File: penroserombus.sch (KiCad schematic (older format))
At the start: 11 parts, among them J1 Conn_01x03_Female, J2 Conn_01x03_Female, J3 Conn_01x03_Male, J4 Conn_01x03_Male, SW1 SW_DPDT_x2

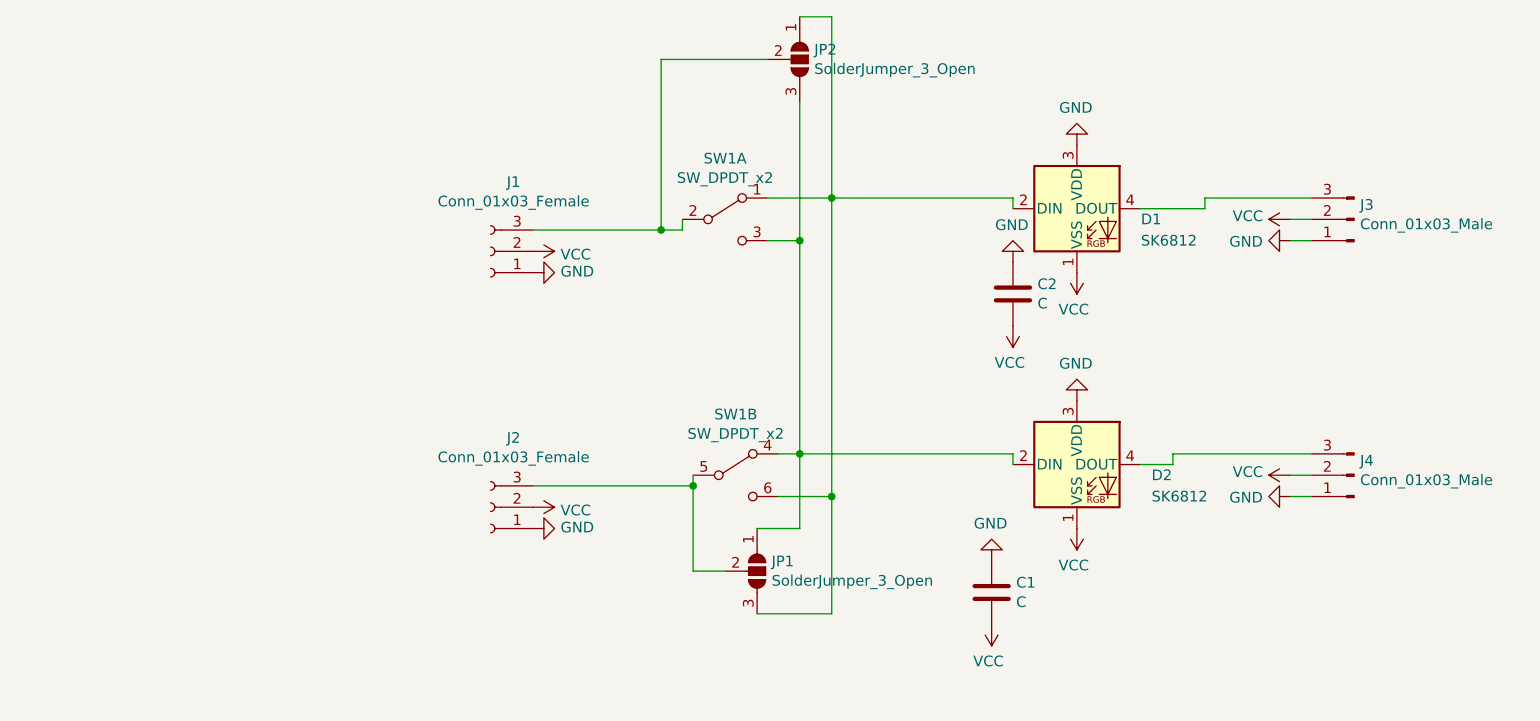
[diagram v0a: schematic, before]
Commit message: board has 4 leds instead of 2.
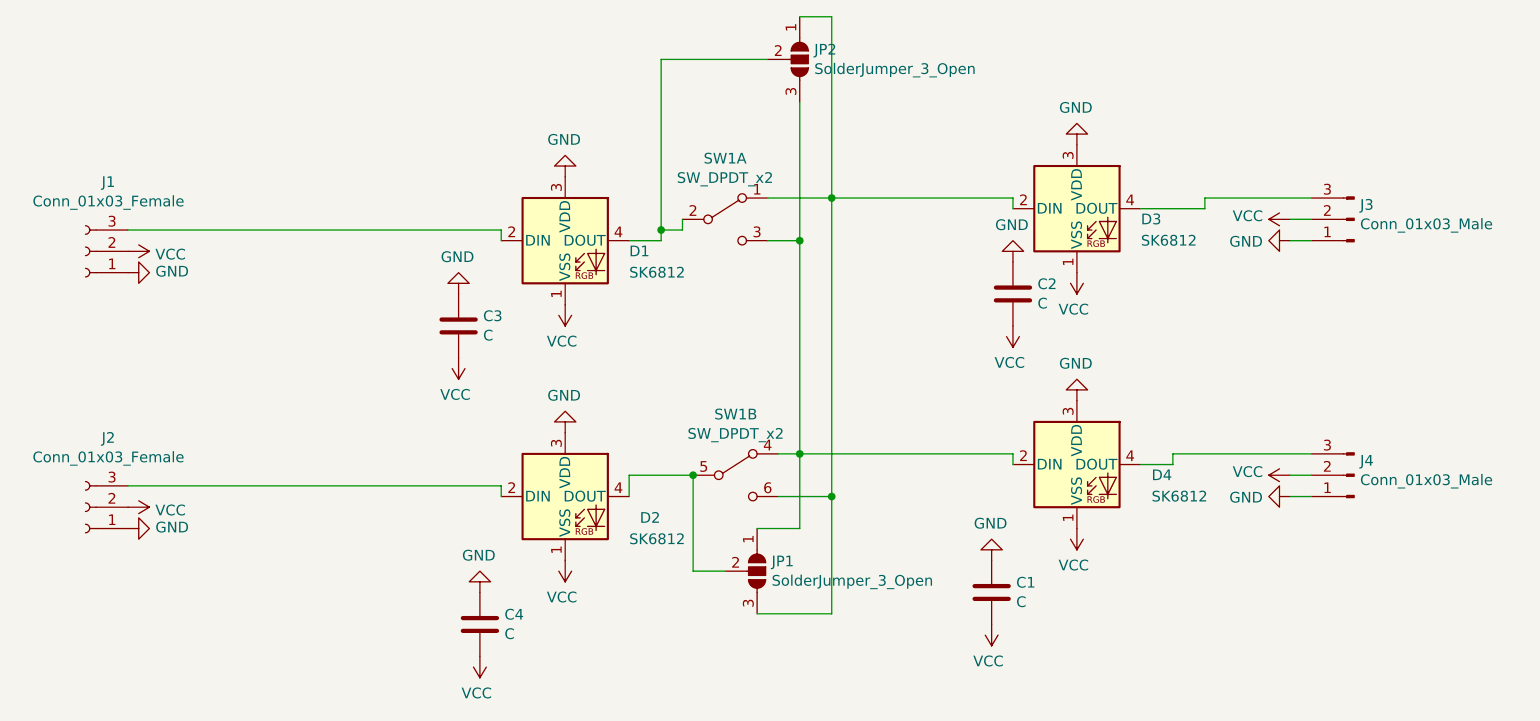
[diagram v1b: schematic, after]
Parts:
- added C3, C4: C, Capacitor_SMD:C_0805_2012Metric_Pad1.18x1.45mm_HandSolder, symbol Device:C
- added D1, D2: SK6812, LED_SMD:LED_SK6812_PLCC4_5.0x5.0mm_P3.2mm, symbol LED:SK6812
- renumbered D1 to D3, D2 to D4
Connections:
- net GND: now also C3.1, C4.1, D1.3 (VDD), D2.3 (VDD)
- net VCC: now also C3.2, C4.2, D1.1 (VSS), D2.1 (VSS)
- net at JP1.2 (C), SW1.5 (B): now also D2.4 (DOUT); no longer J2.3 (Pin_3)
- net at JP2.2 (C), SW1.2 (B): now also D1.4 (DOUT); no longer J1.3 (Pin_3)
- new net: D2.2 (DIN), J2.3 (Pin_3)
- new net: D1.2 (DIN), J1.3 (Pin_3)
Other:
- moved on the sheet: J1, J2
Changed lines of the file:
@@
 $EndDescr
 $Comp
-L LED:SK6812 D1
+L LED:SK6812 D3
 U 1 1 5FB004B1
 P 8050 3200
-F 0 "D1" H 8350 3150 50  0000 L CNN
+F 0 "D3" H 8350 3150 50  0000 L CNN
 F 1 "SK6812" H 8350 3050 50  0000 L CNN
 F 2 "LED_SMD:LED_SK6812_PLCC4_5.0x5.0mm_P3.2mm" H 8100 2900 50  0001 L TNN
@@
 $EndComp
 $Comp
-L LED:SK6812 D2
+L LED:SK6812 D4
 U 1 1 5FB01459
 P 8050 4400
-F 0 "D2" H 8400 4350 50  0000 L CNN
+F 0 "D4" H 8400 4350 50  0000 L CNN
 F 1 "SK6812" H 8400 4250 50  0000 L CNN
 F 2 "LED_SMD:LED_SK6812_PLCC4_5.0x5.0mm_P3.2mm" H 8100 4100 50  0001 L TNN
@@
 L Connector:Conn_01x03_Female J2
 U 1 1 5FB08EB1
-P 5300 4600
-F 0 "J2" H 5192 4275 50  0000 C CNN
-F 1 "Conn_01x03_Female" H 5192 4366 50  0000 C CNN
-F 2 "Connector_PinSocket_2.54mm:PinSocket_1x03_P2.54mm_Vertical" H 5300 4600 50  0001 C CNN
-F 3 "~" H 5300 4600 50  0001 C CNN
-	1    5300 4600
+P 3400 4600
+F 0 "J2" H 3292 4275 50  0000 C CNN
+F 1 "Conn_01x03_Female" H 3292 4366 50  0000 C CNN
+F 2 "Connector_PinSocket_2.54mm:PinSocket_1x03_P2.54mm_Vertical" H 3400 4600 50  0001 C CNN
+F 3 "~" H 3400 4600 50  0001 C CNN
+	1    3400 4600
 	-1   0    0    1
 $EndComp
@@
 L Connector:Conn_01x03_Female J1
 U 1 1 5FB0A86D
-P 5300 3400
-F 0 "J1" H 5192 3075 50  0000 C CNN
-F 1 "Conn_01x03_Female" H 5192 3166 50  0000 C CNN
-F 2 "Connector_PinSocket_2.54mm:PinSocket_1x03_P2.54mm_Vertical" H 5300 3400 50  0001 C CNN
-F 3 "~" H 5300 3400 50  0001 C CNN
-	1    5300 3400
+P 3400 3400
+F 0 "J1" H 3292 3075 50  0000 C CNN
+F 1 "Conn_01x03_Female" H 3292 3166 50  0000 C CNN
+F 2 "Connector_PinSocket_2.54mm:PinSocket_1x03_P2.54mm_Vertical" H 3400 3400 50  0001 C CNN
+F 3 "~" H 3400 3400 50  0001 C CNN
+	1    3400 3400
 	-1   0    0    1
 $EndComp
@@
 L power:GND #PWR0109
 U 1 1 5FB151BF
-P 5500 3500
-F 0 "#PWR0109" H 5500 3250 50  0001 C CNN
-F 1 "GND" V 5505 3372 50  0000 R CNN
-F 2 "" H 5500 3500 50  0001 C CNN
-F 3 "" H 5500 3500 50  0001 C CNN
-	1    5500 3500
+P 3600 3500
+F 0 "#PWR0109" H 3600 3250 50  0001 C CNN
+F 1 "GND" V 3605 3372 50  0000 R CNN
+F 2 "" H 3600 3500 50  0001 C CNN
+F 3 "" H 3600 3500 50  0001 C CNN
+	1    3600 3500
 	0    -1   -1   0
 $EndComp
@@
 L power:VCC #PWR0110
 U 1 1 5FB157FC
-P 5500 3400
-F 0 "#PWR0110" H 5500 3250 50  0001 C CNN
-F 1 "VCC" V 5515 3528 50  0000 L CNN
-F 2 "" H 5500 3400 50  0001 C CNN
-F 3 "" H 5500 3400 50  0001 C CNN
-	1    5500 3400
+P 3600 3400
+F 0 "#PWR0110" H 3600 3250 50  0001 C CNN
+F 1 "VCC" V 3615 3528 50  0000 L CNN
+F 2 "" H 3600 3400 50  0001 C CNN
+F 3 "" H 3600 3400 50  0001 C CNN
+	1    3600 3400
 	0    1    1    0
 $EndComp
@@
 L power:GND #PWR0111
 U 1 1 5FB15E92
-P 5500 4700
-F 0 "#PWR0111" H 5500 4450 50  0001 C CNN
-F 1 "GND" V 5505 4572 50  0000 R CNN
-F 2 "" H 5500 4700 50  0001 C CNN
-F 3 "" H 5500 4700 50  0001 C CNN
-	1    5500 4700
+P 3600 4700
+F 0 "#PWR0111" H 3600 4450 50  0001 C CNN
+F 1 "GND" V 3605 4572 50  0000 R CNN
+F 2 "" H 3600 4700 50  0001 C CNN
+F 3 "" H 3600 4700 50  0001 C CNN
+	1    3600 4700
 	0    -1   -1   0
 $EndComp
@@
 L power:VCC #PWR0112
 U 1 1 5FB162BC
-P 5500 4600
-F 0 "#PWR0112" H 5500 4450 50  0001 C CNN
-F 1 "VCC" V 5515 4728 50  0000 L CNN
-F 2 "" H 5500 4600 50  0001 C CNN
-F 3 "" H 5500 4600 50  0001 C CNN
-	1    5500 4600
+P 3600 4600
+F 0 "#PWR0112" H 3600 4450 50  0001 C CNN
+F 1 "VCC" V 3615 4728 50  0000 L CNN
+F 2 "" H 3600 4600 50  0001 C CNN
+F 3 "" H 3600 4600 50  0001 C CNN
+	1    3600 4600
 	0    1    1    0
 $EndComp
@@
 	1    0    0    -1
 $EndComp
-Wire Wire Line
-	6250 4500 6250 4450
 Wire Wire Line
 	6650 4350 6750 4350
@@
 Wire Wire Line
 	6100 3300 6100 2500
-Connection ~ 6100 3300
 Wire Wire Line
 	6100 3300 6200 3300
@@
 $EndComp
 Wire Wire Line
-	6250 4500 6250 4900
-Wire Wire Line
 	6250 4900 6400 4900
-Connection ~ 6250 4500
 Wire Wire Line
 	6550 4700 6750 4700
@@
 Connection ~ 6900 4550
 Wire Wire Line
-	5500 3300 6100 3300
-Wire Wire Line
-	5500 4500 6250 4500
-Wire Wire Line
 	6900 3150 7750 3150
 Wire Wire Line
@@
 Wire Wire Line
 	8500 4400 8500 4350
+Wire Wire Line
+	6250 4450 6250 4900
+$Comp
+L LED:SK6812 D2
+U 1 1 5FFF6894
+P 5650 4550
+F 0 "D2" H 6000 4450 50  0000 L CNN
+F 1 "SK6812" H 5950 4350 50  0000 L CNN
+F 2 "LED_SMD:LED_SK6812_PLCC4_5.0x5.0mm_P3.2mm" H 5700 4250 50  0001 L TNN
+F 3 "https://cdn-shop.adafruit.com/product-files/1138/SK6812+LED+datasheet+.pdf" H 5750 4175 50  0001 L TNN
+	1    5650 4550
+	1    0    0    -1
+$EndComp
+$Comp
+L power:GND #PWR0117
+U 1 1 5FFF689A
+P 5650 3050
+F 0 "#PWR0117" H 5650 2800 50  0001 C CNN
+F 1 "GND" H 5655 2877 50  0000 C CNN
+F 2 "" H 5650 3050 50  0001 C CNN
+F 3 "" H 5650 3050 50  0001 C CNN
+	1    5650 3050
+	-1   0    0    1
+$EndComp
+$Comp
+L power:GND #PWR0118
+U 1 1 5FFF68A0
+P 5650 4250
+F 0 "#PWR0118" H 5650 4000 50  0001 C CNN
+F 1 "GND" H 5655 4077 50  0000 C CNN
+F 2 "" H 5650 4250 50  0001 C CNN
+F 3 "" H 5650 4250 50  0001 C CNN
+	1    5650 4250
+	-1   0    0    1
+$EndComp
+$Comp
+L power:VCC #PWR0119
+U 1 1 5FFF68A6
+P 5650 3650
+F 0 "#PWR0119" H 5650 3500 50  0001 C CNN
+F 1 "VCC" H 5665 3823 50  0000 C CNN
+F 2 "" H 5650 3650 50  0001 C CNN
+F 3 "" H 5650 3650 50  0001 C CNN
+	1    5650 3650
+	-1   0    0    1
+$EndComp
+$Comp
+L power:VCC #PWR0120
+U 1 1 5FFF68AC
+P 5650 4850
+F 0 "#PWR0120" H 5650 4700 50  0001 C CNN
+F 1 "VCC" H 5665 5023 50  0000 C CNN
+F 2 "" H 5650 4850 50  0001 C CNN
+F 3 "" H 5650 4850 50  0001 C CNN
+	1    5650 4850
+	-1   0    0    1
+$EndComp
+$Comp
+L Device:C C4
+U 1 1 5FFF68C4
+P 5250 5150
+F 0 "C4" H 5365 5196 50  0000 L CNN
+F 1 "C" H 5365 5105 50  0000 L CNN
+F 2 "Capacitor_SMD:C_0805_2012Metric_Pad1.18x1.45mm_HandSolder" H 5288 5000 50  0001 C CNN
+F 3 "~" H 5250 5150 50  0001 C CNN
+	1    5250 5150
+	1    0    0    -1
+$EndComp
+$Comp
+L power:GND #PWR0121
+U 1 1 5FFF68CA
+P 5250 5000
+F 0 "#PWR0121" H 5250 4750 50  0001 C CNN
+F 1 "GND" H 5255 4827 50  0000 C CNN
+F 2 "" H 5250 5000 50  0001 C CNN
+F 3 "" H 5250 5000 50  0001 C CNN
+	1    5250 5000
+	-1   0    0    1
+$EndComp
+$Comp
+L power:VCC #PWR0122
+U 1 1 5FFF68D0
+P 5250 5300
+F 0 "#PWR0122" H 5250 5150 50  0001 C CNN
+F 1 "VCC" H 5265 5473 50  0000 C CNN
+F 2 "" H 5250 5300 50  0001 C CNN
+F 3 "" H 5250 5300 50  0001 C CNN
+	1    5250 5300
+	-1   0    0    1
+$EndComp
+Wire Wire Line
+	5350 3300 5350 3350
+Wire Wire Line
+	5350 4500 5350 4550
+Wire Wire Line
+	3600 4500 5350 4500
+Wire Wire Line
+	5950 3350 6100 3350
+Wire Wire Line
+	6100 3350 6100 3300
+Connection ~ 6100 3300
+Wire Wire Line
+	5950 4550 5950 4450
+Wire Wire Line
+	5950 4450 6250 4450
+Connection ~ 6250 4450
+Wire Wire Line
+	3600 3300 5350 3300
+$Comp
+L power:VCC #PWR0123
+U 1 1 5FFF68BE
+P 5150 3900
+F 0 "#PWR0123" H 5150 3750 50  0001 C CNN
+F 1 "VCC" H 5165 4073 50  0000 C CNN
+F 2 "" H 5150 3900 50  0001 C CNN
+F 3 "" H 5150 3900 50  0001 C CNN
+	1    5150 3900
+	-1   0    0    1
+$EndComp
+$Comp
+L power:GND #PWR0124
+U 1 1 5FFF68B8
+P 5150 3600
+F 0 "#PWR0124" H 5150 3350 50  0001 C CNN
+F 1 "GND" H 5155 3427 50  0000 C CNN
+F 2 "" H 5150 3600 50  0001 C CNN
+F 3 "" H 5150 3600 50  0001 C CNN
+	1    5150 3600
+	-1   0    0    1
+$EndComp
+$Comp
+L Device:C C3
+U 1 1 5FFF68B2
+P 5150 3750
+F 0 "C3" H 5265 3796 50  0000 L CNN
+F 1 "C" H 5265 3705 50  0000 L CNN
+F 2 "Capacitor_SMD:C_0805_2012Metric_Pad1.18x1.45mm_HandSolder" H 5188 3600 50  0001 C CNN
+F 3 "~" H 5150 3750 50  0001 C CNN
+	1    5150 3750
+	1    0    0    -1
+$EndComp
+$Comp
+L LED:SK6812 D1
+U 1 1 5FFF688E
+P 5650 3350
+F 0 "D1" H 5950 3300 50  0000 L CNN
+F 1 "SK6812" H 5950 3200 50  0000 L CNN
+F 2 "LED_SMD:LED_SK6812_PLCC4_5.0x5.0mm_P3.2mm" H 5700 3050 50  0001 L TNN
+F 3 "https://cdn-shop.adafruit.com/product-files/1138/SK6812+LED+datasheet+.pdf" H 5750 2975 50  0001 L TNN
+	1    5650 3350
+	1    0    0    -1
+$EndComp
 $EndSCHEMATC

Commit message: added kite and dart tiling
idk why im doing this
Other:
- note added: "Port A"
- note added: "Port T"
- note added: "port C"
- note added: "port G"
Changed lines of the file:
@@
 	1    0    0    -1
 $EndComp
+Text Notes 3450 4900 0    50   ~ 0
+port G
+Text Notes 9250 4750 0    50   ~ 0
+port C
+Text Notes 3400 3750 0    50   ~ 0
+Port A
+Text Notes 9250 3600 0    50   ~ 0
+Port T
 $EndSCHEMATC
